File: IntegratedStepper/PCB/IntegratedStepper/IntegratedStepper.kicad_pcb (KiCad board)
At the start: 4 copper layers, 57 x 42.5 mm, 76 parts, among them IC1 DRV8844PWPR, IC2 SN65HVD230DR, IC3 LMR38020FSQDDARQ1, J1 8P8C, J2 8P8C, J3 Screw_Terminal_01x02, J4 Screw_Terminal_01x02, J5 Conn_01x05_Socket, Q1 SS8050-G, Q2 SS8050-G, U1 ESP32-WROOM-32E, U2 AS5048A, U3 CP2102N-Axx-xQFN28

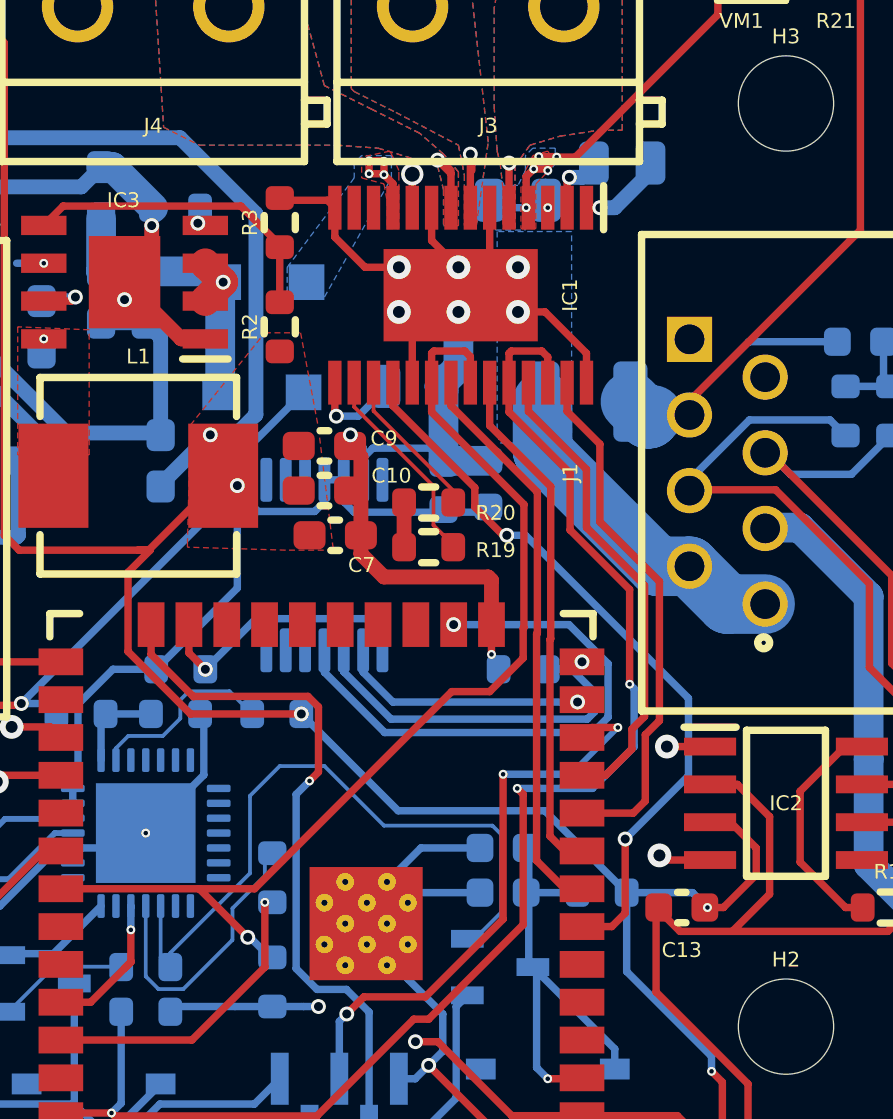
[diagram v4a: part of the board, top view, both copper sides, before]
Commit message: add silkscreen text
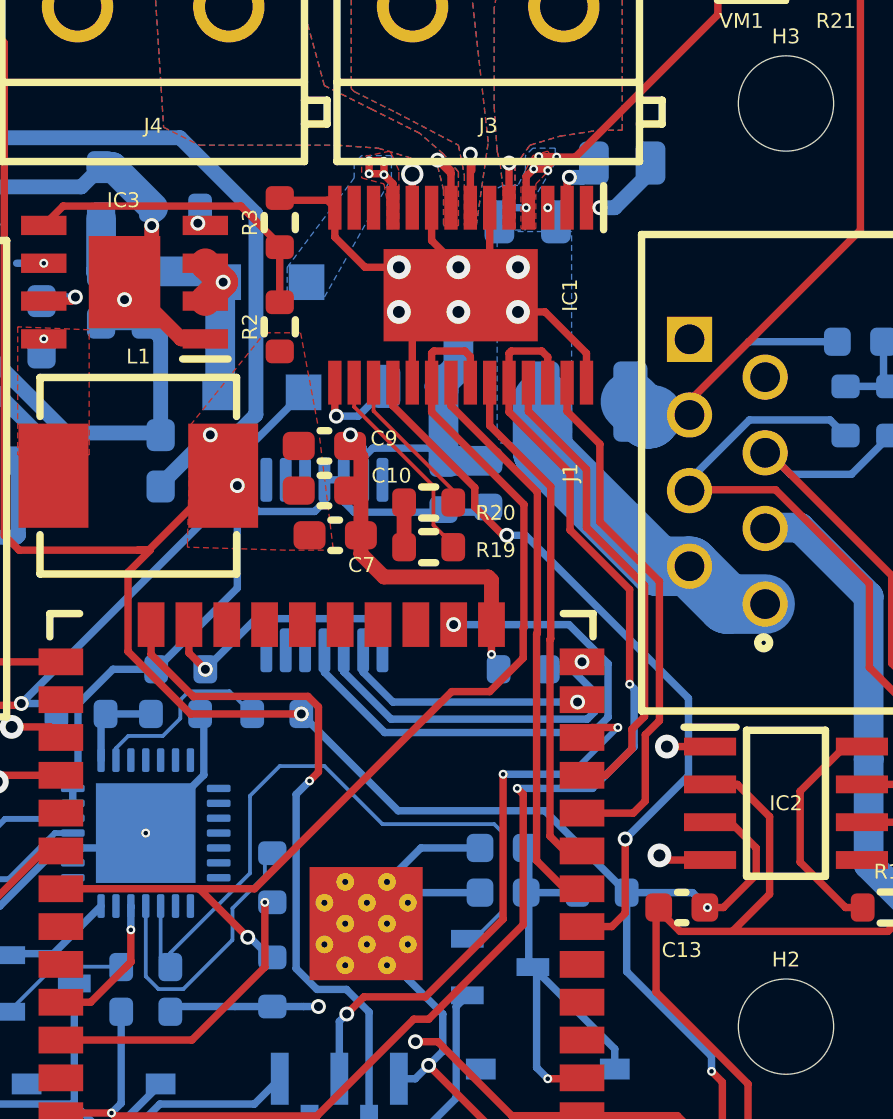
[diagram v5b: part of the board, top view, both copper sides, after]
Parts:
- moved C2 0.79 mm to (127.8, 109.5)
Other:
- board text added: "Integrated Stepper"
- board text added: "v1.0, 3/2024"
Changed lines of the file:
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@@
 	(footprint "Capacitor_SMD:C_0805_2012Metric"
 		(layer "B.Cu")
-		(at 127.5 108.75)
+		(at 127.825 109.475)
 		(descr "Capacitor SMD 0805 (2012 Metric), square (rectangular) end terminal, IPC_7351 nominal, (Body size source: IPC-SM-782 page 76, https://www.pcb-3d.com/wordpress/wp-content/uploads/ipc-sm-782a_amendment_1_and_2.pdf, https://docs.google.com/spreadsheets/d/1BsfQQcO9C6DZCsRaXUlFlo91Tg2WpOkGARC1WS5S8t0/edit?usp=sharing), generated with kicad-footprint-generator")
 		(tags "capacitor")
@@
 		)
 	)
+	(gr_text "Integrated Stepper "
+		(at 143.1 127.8 0)
+		(layer "B.SilkS")
+		(effects
+			(font
+				(size 0.5 0.5)
+				(thickness 0.15)
+			)
+			(justify left bottom mirror)
+		)
+	)
 	(gr_text "O4"
 		(at 111.5 105 0)
@@
 		)
 	)
+	(gr_text "v1.0, 3/2024"
+		(at 143.1 128.6 0)
+		(layer "B.SilkS")
+		(effects
+			(font
+				(size 0.5 0.5)
+				(thickness 0.15)
+			)
+			(justify left bottom mirror)
+		)
+	)
 	(gr_text "O2"
 		(at 123 105 0)
@@
 	)
 	(segment
-		(start 125.8 133.55)
-		(end 126.05 133.55)
+		(start 115.825 134.025)
+		(end 115.825 134.5)
 		(width 0.127)
 		(layer "B.Cu")
@@
 	)
 	(segment
-		(start 126.05 133.55)
-		(end 126.9385 132.6615)
+		(start 119.5 127.75)
+		(end 118.5 128.75)
 		(width 0.127)
 		(layer "B.Cu")
@@
 	)
 	(segment
-		(start 115.825 134.025)
-		(end 115.825 134.5)
+		(start 118.5 131.35)
+		(end 115.825 134.025)
 		(width 0.127)
 		(layer "B.Cu")
@@
 	)
 	(segment
-		(start 126.9385 132.6615)
-		(end 126.9385 130.048398)
+		(start 118.5 128.75)
+		(end 118.5 131.35)
 		(width 0.127)
 		(layer "B.Cu")
@@
 	)
 	(segment
-		(start 121 127.75)
-		(end 119.5 127.75)
+		(start 115.825 134.5)
+		(end 115.5 134.175)
 		(width 0.127)
 		(layer "B.Cu")
@@
 	)
 	(segment
-		(start 115.825 134.5)
-		(end 115.5 134.175)
+		(start 126.05 133.55)
+		(end 127 132.6)
 		(width 0.127)
 		(layer "B.Cu")
@@
 	)
 	(segment
-		(start 119.5 127.75)
-		(end 118.5 128.75)
+		(start 115.5 134.175)
+		(end 115.5 132.45)
 		(width 0.127)
 		(layer "B.Cu")
@@
 	)
 	(segment
-		(start 118.5 131.35)
-		(end 115.825 134.025)
+		(start 121 127.75)
+		(end 119.5 127.75)
 		(width 0.127)
 		(layer "B.Cu")
@@
 	)
 	(segment
-		(start 115.5 134.175)
-		(end 115.5 132.45)
+		(start 125.8 133.55)
+		(end 126.05 133.55)
 		(width 0.127)
 		(layer "B.Cu")
@@
 	)
 	(segment
-		(start 118.5 128.75)
-		(end 118.5 131.35)
+		(start 127 132.6)
+		(end 127 130)
 		(width 0.127)
 		(layer "B.Cu")
@@
 	)
 	(segment
-		(start 126.640102 129.75)
-		(end 123 129.75)
+		(start 122.95 129.7)
+		(end 121 127.75)
 		(width 0.127)
 		(layer "B.Cu")
@@
 	)
 	(segment
-		(start 126.9385 130.048398)
-		(end 126.640102 129.75)
+		(start 127 130)
+		(end 126.7 129.7)
 		(width 0.127)
 		(layer "B.Cu")
@@
 	)
 	(segment
-		(start 123 129.75)
-		(end 121 127.75)
+		(start 126.7 129.7)
+		(end 122.95 129.7)
 		(width 0.127)
 		(layer "B.Cu")

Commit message: add 3D model
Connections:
- net /DRV8844/EN2 renamed /DRV8844/EN1
- J5 pad 1: V_USB -> 3V3_VCC
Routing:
- net V_USB: track 62.4 -> 48.8 mm, vias 2 -> 1
- net GND: track 272.2 -> 269.7 mm
- net unconnected-(IC3-PG-Pad6): track 0.91 -> 0.00 mm, vias 1 -> 0
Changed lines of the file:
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@@
 	(net 115 "unconnected-(USBC1-PadA2)")
 	(net 116 "unconnected-(IC3-PG-Pad6)")
-	(net 117 "/DRV8844/EN2")
+	(net 117 "/DRV8844/EN1")
 	(net 118 "/DRV8844/EN4")
 	(footprint "Capacitor_SMD:C_0603_1608Metric_Pad1.08x0.95mm_HandSolder"
@@
 			(size 0.45 1.475)
 			(layers "F.Cu" "F.Paste" "F.Mask")
-			(net 117 "/DRV8844/EN2")
+			(net 117 "/DRV8844/EN1")
 			(pinfunction "EN2")
 			(pintype "passive")
@@
 			(size 0.45 1.475)
 			(layers "F.Cu" "F.Paste" "F.Mask")
-			(net 117 "/DRV8844/EN2")
+			(net 117 "/DRV8844/EN1")
 			(pinfunction "EN1")
 			(pintype "passive")
@@
 			)
 		)
+		(property "LCSC" "C12084"
+			(at 0 0 0)
+			(unlocked yes)
+			(layer "F.Fab")
+			(hide yes)
+			(effects
+				(font
+					(size 1 1)
+					(thickness 0.15)
+				)
+			)
+		)
+		(property "LCSC Part" "C12084"
+			(at 0 0 0)
+			(unlocked yes)
+			(layer "F.Fab")
+			(hide yes)
+			(effects
+				(font
+					(size 1 1)
+					(thickness 0.15)
+				)
+			)
+		)
+		(property "LCSC Part Number" "C12084"
+			(at 0 0 0)
+			(unlocked yes)
+			(layer "F.Fab")
+			(hide yes)
+			(effects
+				(font
+					(size 1 1)
+					(thickness 0.15)
+				)
+			)
+		)
 		(sheetname "CAN_Transciever")
 		(sheetfile "RS485.kicad_sch")
@@
 		(tags "Capacitor Polarised")
 		(property "Reference" "C29"
-			(at 0 0 -90)
+			(at -1.9 -3.35 270)
 			(layer "F.SilkS")
 			(effects
 				(font
-					(size 1.27 1.27)
-					(thickness 0.254)
+					(size 0.5 0.5)
+					(thickness 0.125)
 				)
 			)
@@
 		(tags "Capacitor Polarised")
 		(property "Reference" "C28"
-			(at 0 0 -90)
+			(at -2.15 -3 270)
 			(layer "F.SilkS")
 			(effects
 				(font
-					(size 1.27 1.27)
-					(thickness 0.254)
+					(size 0.5 0.5)
+					(thickness 0.125)
 				)
 			)
@@
 			(size 1.5 0.9)
 			(layers "F.Cu" "F.Paste" "F.Mask")
-			(net 117 "/DRV8844/EN2")
+			(net 117 "/DRV8844/EN1")
 			(pinfunction "IO23")
 			(pintype "bidirectional")
@@
 			(layers "B.Cu" "B.Paste" "B.Mask")
 			(roundrect_rratio 0.25)
-			(net 117 "/DRV8844/EN2")
+			(net 117 "/DRV8844/EN1")
 			(pintype "passive")
 		)
@@
 			(size 1.75 0.6)
 			(layers "B.Cu" "B.Paste" "B.Mask")
-			(net 101 "V_USB")
+			(net 8 "3V3_VCC")
 			(pinfunction "Pin_1")
 			(pintype "passive")
@@
 	)
 	(segment
-		(start 108.225 104.47)
-		(end 108.225 106.98)
-		(width 0.5)
-		(layer "B.Cu")
-		(net 5)
-	)
-	(segment
 		(start 122.3 117.400001)
 		(end 122.625001 117.075)
@@
 	)
 	(segment
+		(start 119.5 138.25)
+		(end 119.5 136.075)
+		(width 0.25)
+		(layer "B.Cu")
+		(net 8)
+	)
+	(segment
 		(start 122.000001 119.225)
 		(end 125 119.225)
@@
 	)
 	(segment
-		(start 109.775 106.98)
-		(end 109.775 104.47)
-		(width 0.5)
-		(layer "B.Cu")
-		(net 8)
-	)
-	(segment
 		(start 118.7 109.2)
 		(end 118.7 115.95)
@@
 	)
 	(segment
+		(start 119.5 136.075)
+		(end 119.25 135.825)
+		(width 0.25)
+		(layer "B.Cu")
+		(net 8)
+	)
+	(segment
 		(start 118 135.825)
 		(end 116 135.825)
@@
 	)
 	(segment
+		(start 115.18 124)
+		(end 116.59 125.41)
+		(width 0.25)
+		(layer "F.Cu")
+		(net 42)
+	)
+	(segment
 		(start 120.8 125.761827)
 		(end 120.448173 125.41)
@@
 		(net 42)
 	)
-	(segment
-		(start 115.18 124)
-		(end 116.59 125.41)
-		(width 0.25)
-		(layer "F.Cu")
-		(net 42)
-	)
 	(via
 		(at 120.5 128.25)
@@
 	)
 	(segment
-		(start 120.5 128.25)
-		(end 120.05 128.7)
+		(start 121.738173 135.25)
+		(end 122.5 136.011827)
 		(width 0.25)
 		(layer "B.Cu")
@@
 	)
 	(segment
-		(start 120.75 135.25)
-		(end 121.738173 135.25)
+		(start 120.05 134.95)
+		(end 120.35 135.25)
 		(width 0.25)
 		(layer "B.Cu")
@@
 	)
 	(segment
-		(start 121.738173 135.25)
-		(end 122.5 136.011827)
+		(start 120.05 128.7)
+		(end 120.05 134.95)
 		(width 0.25)
 		(layer "B.Cu")
@@
 	)
 	(segment
-		(start 120.05 128.7)
-		(end 120.05 134.55)
+		(start 120.35 135.25)
+		(end 121.738173 135.25)
 		(width 0.25)
 		(layer "B.Cu")
@@
 	)
 	(segment
-		(start 120.05 134.55)
-		(end 120.75 135.25)
+		(start 122.5 136.011827)
+		(end 122.5 140)
 		(width 0.25)
 		(layer "B.Cu")
@@
 	)
 	(segment
-		(start 122.5 136.011827)
-		(end 122.5 140)
+		(start 120.5 128.25)
+		(end 120.05 128.7)
 		(width 0.25)
 		(layer "B.Cu")
@@
 	)
 	(segment
-		(start 113.9 141.6)
-		(end 108.675 141.6)
-		(width 0.25)
-		(layer "F.Cu")
-		(net 101)
-	)
-	(segment
 		(start 103.375 131.925)
 		(end 103.64 131.66)
@@
 	)
 	(segment
-		(start 114.5 141)
-		(end 113.9 141.6)
-		(width 0.25)
-		(layer "F.Cu")
-		(net 101)
-	)
-	(segment
 		(start 105.849695 126.225)
 		(end 106.975 126.225)
@@
 	)
 	(segment
-		(start 114.5 140.5)
-		(end 114.5 141)
-		(width 0.25)
-		(layer "F.Cu")
-		(net 101)
-	)
-	(segment
 		(start 106.14 128.82)
 		(end 106.14 128.045)
@@
 	)
 	(segment
-		(start 108.675 141.6)
-		(end 108.075 141)
-		(width 0.25)
-		(layer "F.Cu")
-		(net 101)
-	)
-	(segment
 		(start 106.07 127.975)
 		(end 105.751778 127.975)
@@
 	)
 	(via
-		(at 114.5 140.5)
-		(size 0.3)
-		(drill 0.15)
-		(layers "F.Cu" "B.Cu")
-		(net 101)
-	)
-	(via
 		(at 110.820921 125.649354)
 		(size 0.5)
@@
 	)
 	(segment
-		(start 114.5 140.075)
-		(end 115.475 139.1)
-		(width 0.25)
-		(layer "B.Cu")
-		(net 101)
-	)
-	(segment
 		(start 110.820921 125.649354)
 		(end 111.649354 125.649354)
@@
 	)
 	(segment
-		(start 118.65 139.1)
-		(end 119.5 138.25)
-		(width 0.25)
-		(layer "B.Cu")
-		(net 101)
-	)
-	(segment
 		(start 117.5 118)
 		(end 120.3 115.2)
@@
 		(net 101)
 	)
-	(segment
-		(start 115.475 139.1)
-		(end 118.65 139.1)
-		(width 0.25)
-		(layer "B.Cu")
-		(net 101)
-	)
-	(segment
-		(start 114.5 140.5)
-		(end 114.5 140.075)
-		(width 0.25)
-		(layer "B.Cu")
-		(net 101)
-	)
 	(via
 		(at 105.14 130.68)
@@
 		(net 103)
 	)
-	(via
-		(at 111.576 110.865)
-		(size 0.3)
-		(drill 0.15)
-		(layers "F.Cu" "B.Cu")
-		(net 116)
-	)
-	(segment
-		(start 110.665 110.865)
-		(end 111.576 110.865)
-		(width 0.25)
-		(layer "B.Cu")
-		(net 116)
-	)
 	(segment
 		(start 129.25 119.822792)
@@
 	)
 	(zone
-		(net 3)
-		(net_name "VCC")
+		(net 5)
+		(net_name "GND")
 		(layer "B.Cu")
-		(name "VM+")
+		(name "VM-")
 		(hatch edge 0.5)
 		(priority 9)
@@
 	)
 	(zone
-		(net 3)
-		(net_name "VCC")
+		(net 5)
+		(net_name "GND")
 		(layer "B.Cu")
-		(name "VM+")
+		(name "VM-")
 		(hatch edge 0.5)
 		(priority 9)

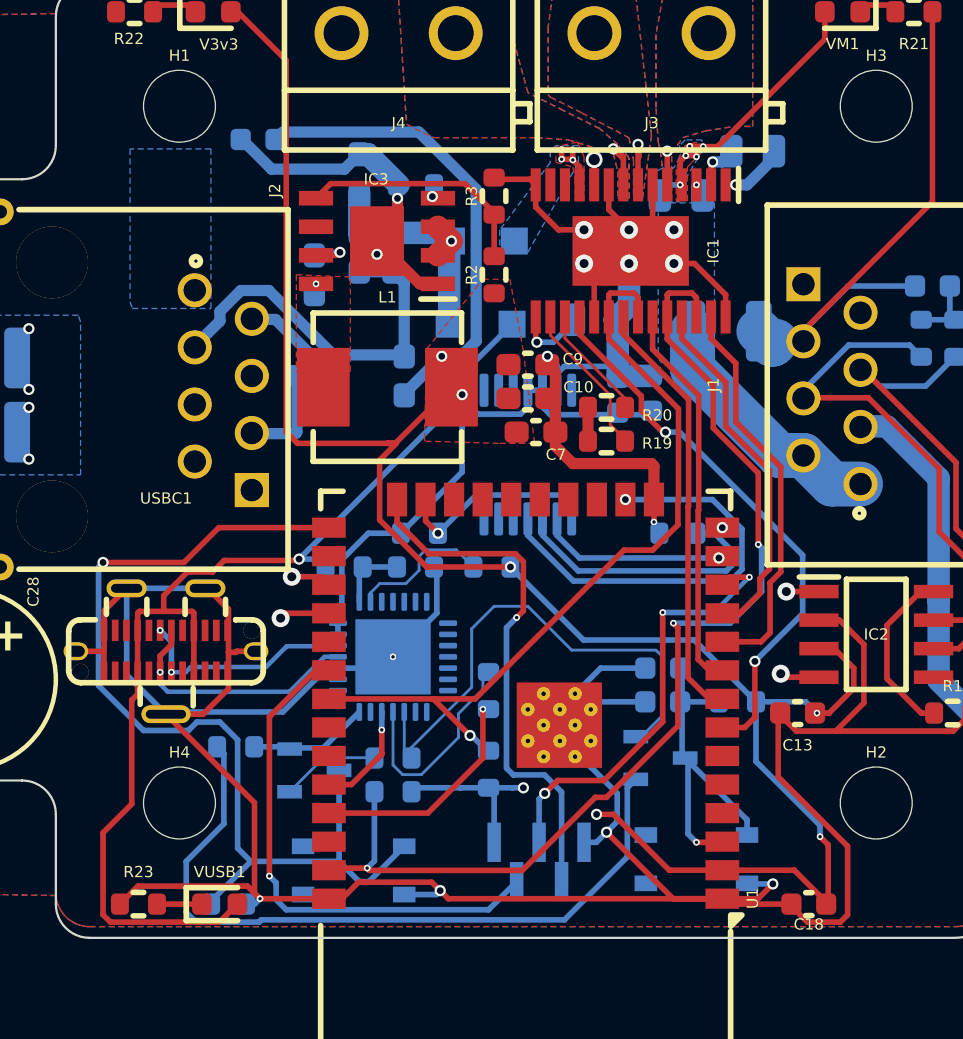
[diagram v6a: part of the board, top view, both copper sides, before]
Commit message: change vias to be larger for cheaper manufacturing
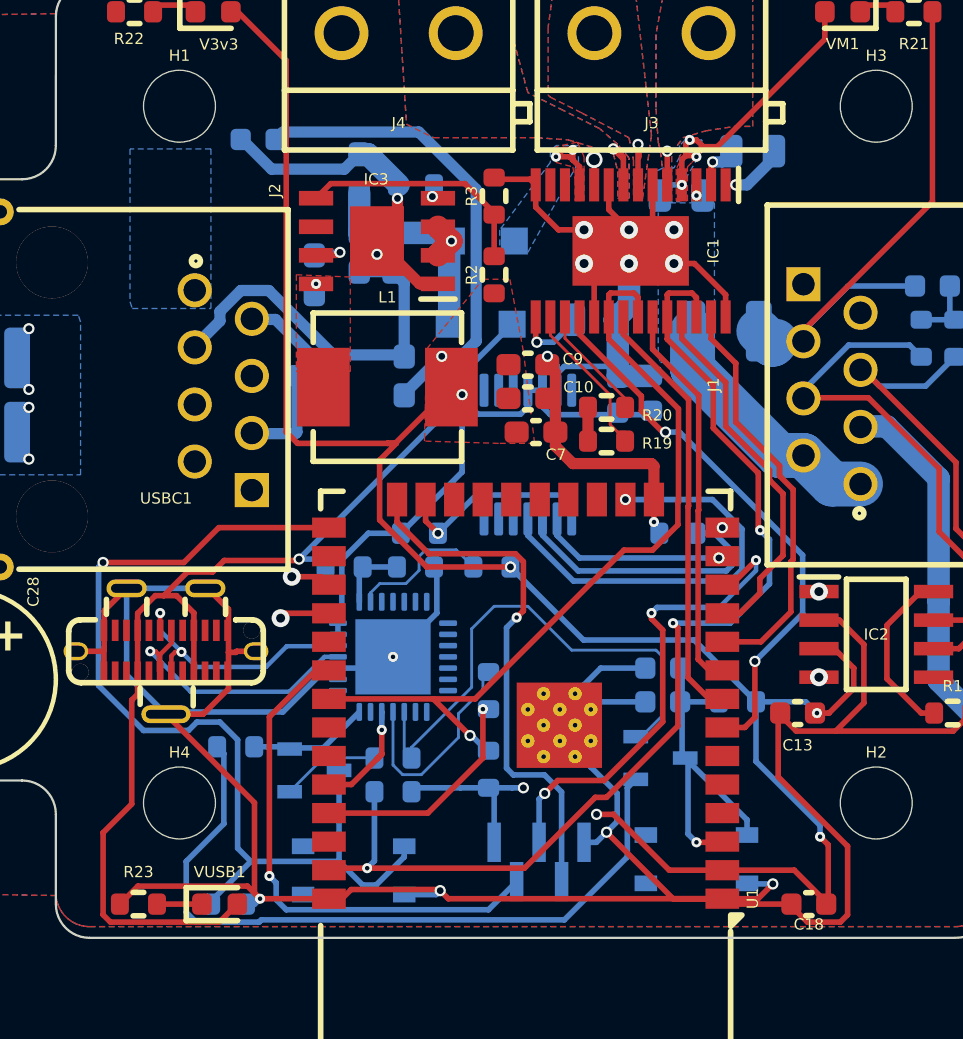
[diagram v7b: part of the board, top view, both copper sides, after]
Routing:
- net /ESP32_MCU/ENC+: track 19.6 -> 21.9 mm
- net USB_D-: track 9.97 -> 11.8 mm
- net USB_D+: track 11.3 -> 13.1 mm
- net /CAN_Transciever/CAN_RX: track 29.2 -> 27.9 mm
- net VCC: track 39.3 -> 40.0 mm, vias 17 -> 13
